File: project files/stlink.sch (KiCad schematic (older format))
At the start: 62 parts, among them J1 USB_C_Receptacle_USB2.0, J2 SWD, J3 SELF, J4 TARGET, Q1 MMBT9013, U1 STM32F103CBTx, U2 AMS1117-3.3, Y1 8MHz

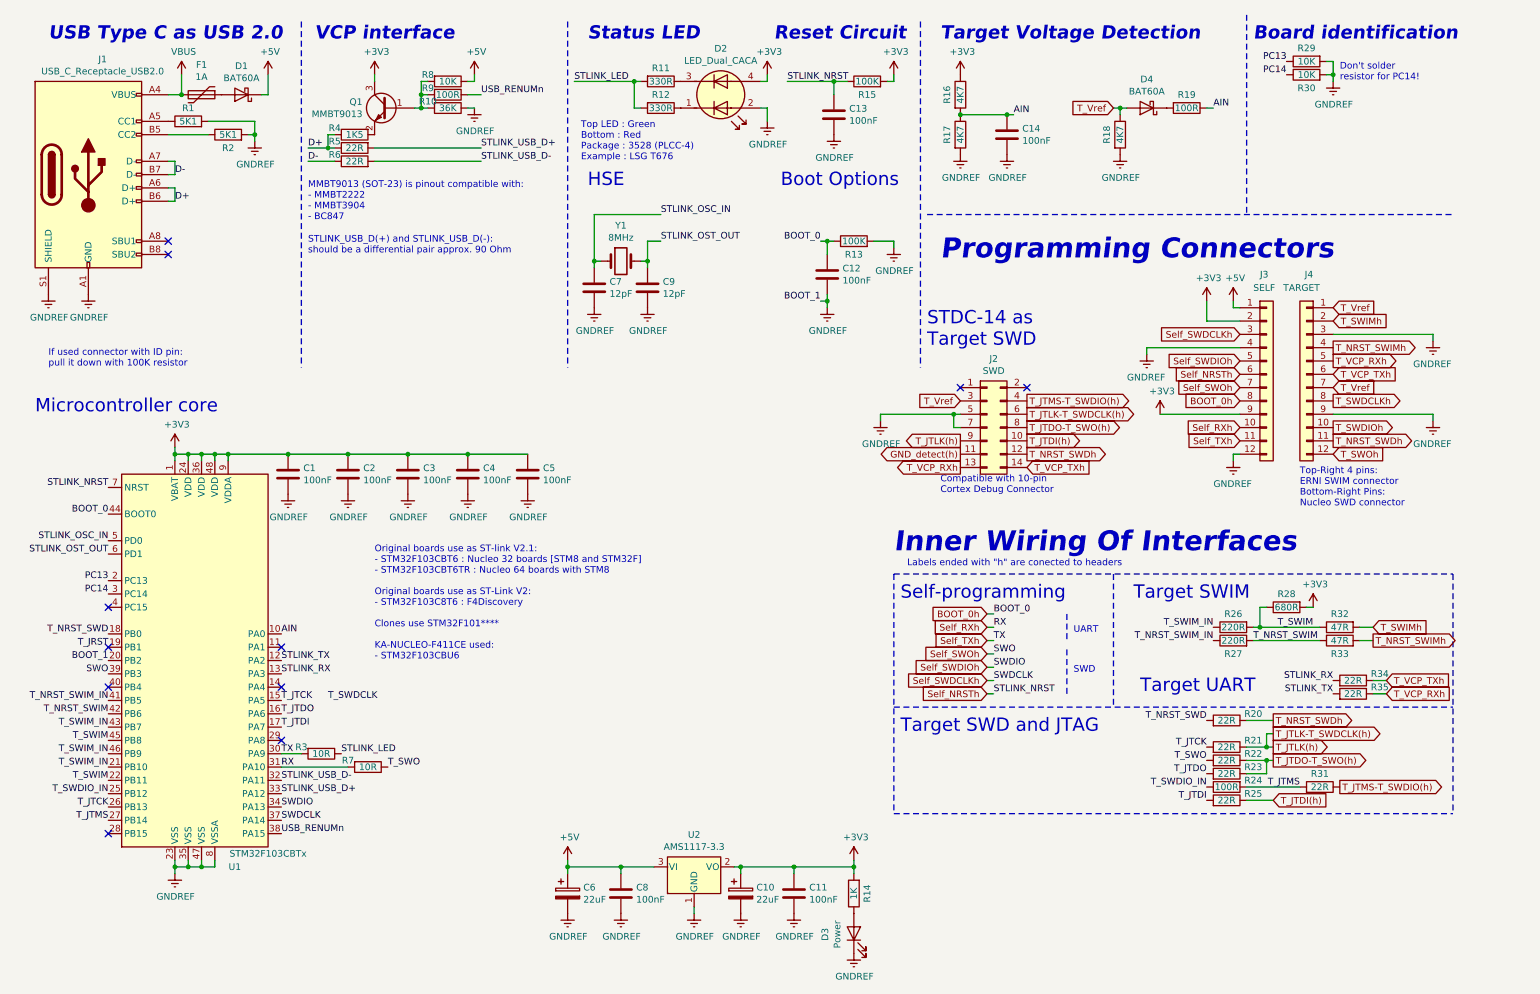
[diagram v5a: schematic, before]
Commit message: USB Type C shield fix
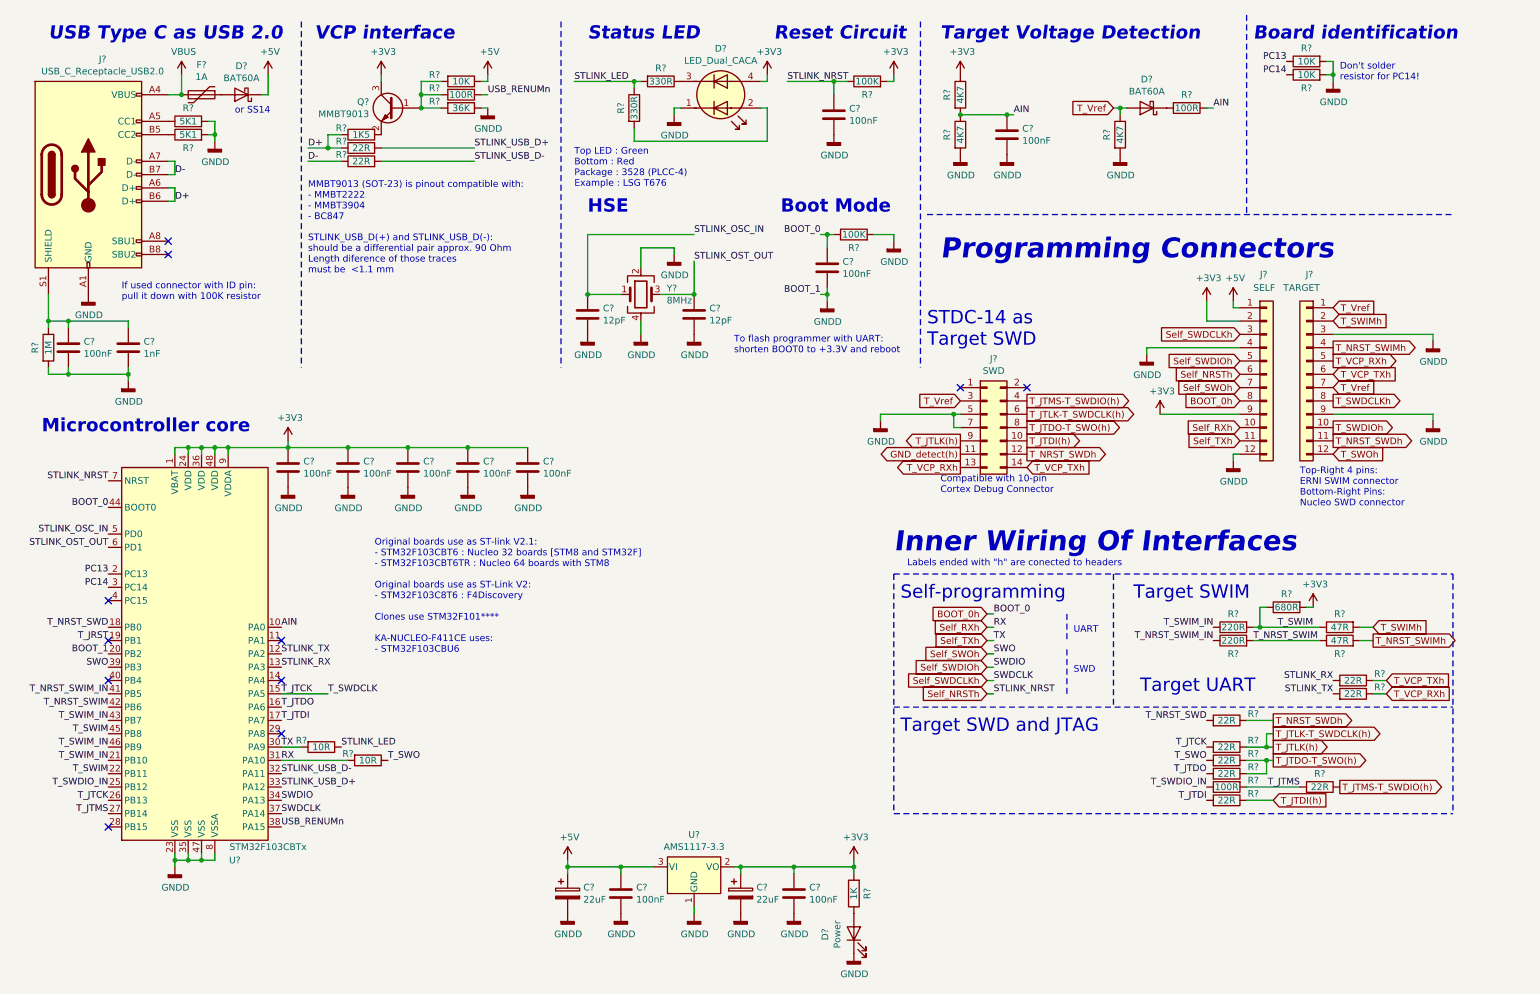
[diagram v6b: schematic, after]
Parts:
- removed Y1: 8MHz, Crystal:Crystal_HC49-4H_Vertical, symbol Device:Crystal
- added C?: 1nF, Capacitor_SMD:C_0603_1608Metric, symbol Device:C
- added C?: 100nF, Capacitor_SMD:C_0603_1608Metric, symbol Device:C
- added R?: 1M, Resistor_SMD:R_0603_1608Metric_Pad1.05x0.95mm_HandSolder, symbol Device:R
- added Y?: 8MHz, Crystal:Crystal_SMD_Abracon_ABM8G-4Pin_3.2x2.5mm, symbol Device:Crystal_GND24
- renumbered C9 to C?, C7 to C?, C13 to C?, C12 to C?, C14 to C?, C1 to C?, C2 to C?, C3 to C?, C4 to C?, C5 to C?, C10 to C?, C6 to C?, C11 to C?, C8 to C?, D3 to D?, D2 to D?, D4 to D?, D1 to D?, F1 to F?, J1 to J?, J2 to J?, J3 to J?, J4 to J?, Q1 to Q?, R2 to R?, R1 to R?, R6 to R?, R5 to R?, R4 to R?, R9 to R?, R8 to R?, R10 to R?, R11 to R?, R12 to R?, R27 to R?, R26 to R?, R33 to R?, R32 to R?, R29 to R?, R15 to R?, R13 to R?, R16 to R?, R17 to R?, R28 to R?, R30 to R?, R18 to R?, R19 to R?, R22 to R?, R31 to R?, R21 to R?, R20 to R?, R24 to R?, R14 to R?, R7 to R?, R3 to R?, R35 to R?, R34 to R?, R23 to R?, R25 to R?, U1 to U?, U2 to U?
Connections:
- net STLINK_LED: now also R?.1; no longer R?.2
- net STLINK_OSC_IN: now also Y?.1
- net STLINK_OST_OUT: now also Y?.3
- net GNDD: now reaches D?.1 (A1)
- net GNDD: now also C?.2, C?.2, C?.2, C?.2, C?.2, C?.2, C?.2, C?.2, C?.2, C?.2, C?.2, C?.2, C?.2, C?.2, D?.1 (K), J?.12 (Pin_12), J?.3 (Pin_3), J?.4 (Pin_4), J?.5 (Pin_5), J?.7 (Pin_7), J?.9 (Pin_9), J?.A1 (GND), J?.A12 (GND), J?.B1 (GND), J?.B12 (GND), R?.1, R?.2, R?.2, R?.2, R?.2, R?.2, R?.2, R?.2, U?.1 (GND), U?.20 (PB2), U?.23 (VSS), U?.35 (VSS), U?.47 (VSS), U?.8 (VSSA), C?.2, C?.2, R?.2, Y?.2, Y?.4; no longer R?.1
- removed net GNDREF: C?.2, C?.2, C?.2, C?.2, C?.2, C?.2, C?.2, C?.2, C?.2, C?.2, C?.2, C?.2, C?.2, C?.2, D?.1 (K), D?.2 (K1), J?.12 (Pin_12), J?.3 (Pin_3), J?.4 (Pin_4), J?.5 (Pin_5), J?.7 (Pin_7), J?.9 (Pin_9), J?.A1 (GND), J?.A12 (GND), J?.B1 (GND), J?.B12 (GND), J?.S1 (SHIELD), R?.1, R?.2, R?.2, R?.2, R?.2, R?.2, R?.2, R?.2, U?.1 (GND), U?.20 (PB2), U?.23 (VSS), U?.35 (VSS), U?.47 (VSS), U?.8 (VSSA)
- new net: C?.1, C?.1, J?.S1 (SHIELD), R?.1
- new net: D?.2 (K1), R?.2
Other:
- note added: "Boot Mode"
- note added: "Original boards use as ST-link V2.1:\n- STM32F103CBT6 : Nucleo 32 boards [STM8 and STM32F]\n- STM32F103CBT6TR : Nucleo 64 boards with STM8\n\nOriginal boards use as ST-Link V2:\n- STM32F103C8T6 : F4Discovery\n\nClones use STM32F101****\n\nKA-NUCLEO-F411CE uses:\n- STM32F103CBU6"
- note added: "STLINK_USB_D(+) and STLINK_USB_D(-):\nshould be a differential pair approx. 90 Ohm\nLength diference of those traces \nmust be <1.1 mm"
- note added: "To flash programmer with UART:\nshorten BOOT0 to +3.3V and reboot"
- note added: "or SS14"
- note removed: "Boot Options"
- note removed: "Original boards use as ST-link V2.1:\n- STM32F103CBT6 : Nucleo 32 boards [STM8 and STM32F]\n- STM32F103CBT6TR : Nucleo 64 boards with STM8\n\nOriginal boards use as ST-Link V2:\n- STM32F103C8T6 : F4Discovery\n\nClones use STM32F101****\n\nKA-NUCLEO-F411CE used:\n- STM32F103CBU6"
- note removed: "STLINK_USB_D(+) and STLINK_USB_D(-):\nshould be a differential pair approx. 90 Ohm"
- moved on the sheet: C?, Q?, R?, U?

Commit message: Update stlink.sch
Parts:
- removed R?: 10K, Resistor_SMD:R_0603_1608Metric_Pad1.05x0.95mm_HandSolder, symbol Device:R
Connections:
- net AIN: now also C?.2; no longer C?.1
- net GNDD: now also C?.1, R?.1; no longer C?.2, R?.2, R?.2
- net PC13: no longer names the net of U?.2 (PC13)
- net PC13: now also R?.2; no longer R?.1
- net PC14: no longer names the net of U?.3 (PC14)
- no-connect marks 11 -> 12
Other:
- note added: "STDC-14 as\nTarget SWD + VCP"
- note added: "Target Voltage\nDetection"
- note removed: "Board identification"
- note removed: "Don't solder\nresistor for PC14!"
- note removed: "STDC-14 as\nTarget SWD"
- note removed: "Target Voltage Detection"
- moved on the sheet: C?, D?, J?, R?, Y?

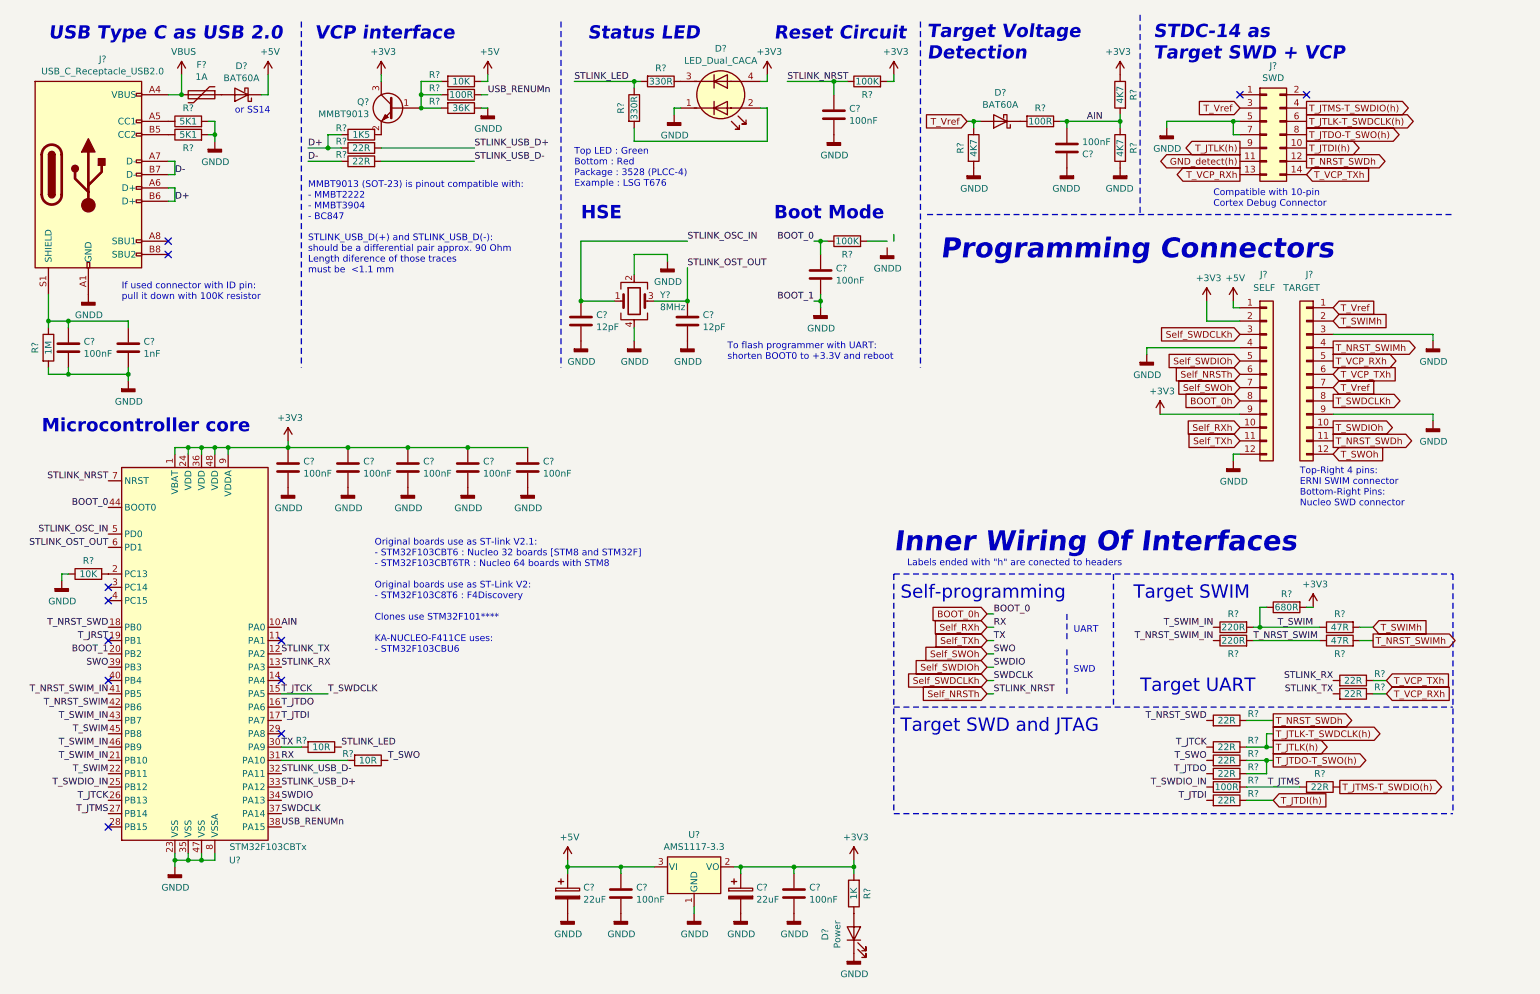
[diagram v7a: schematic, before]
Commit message: Added possibility to power target from programmer
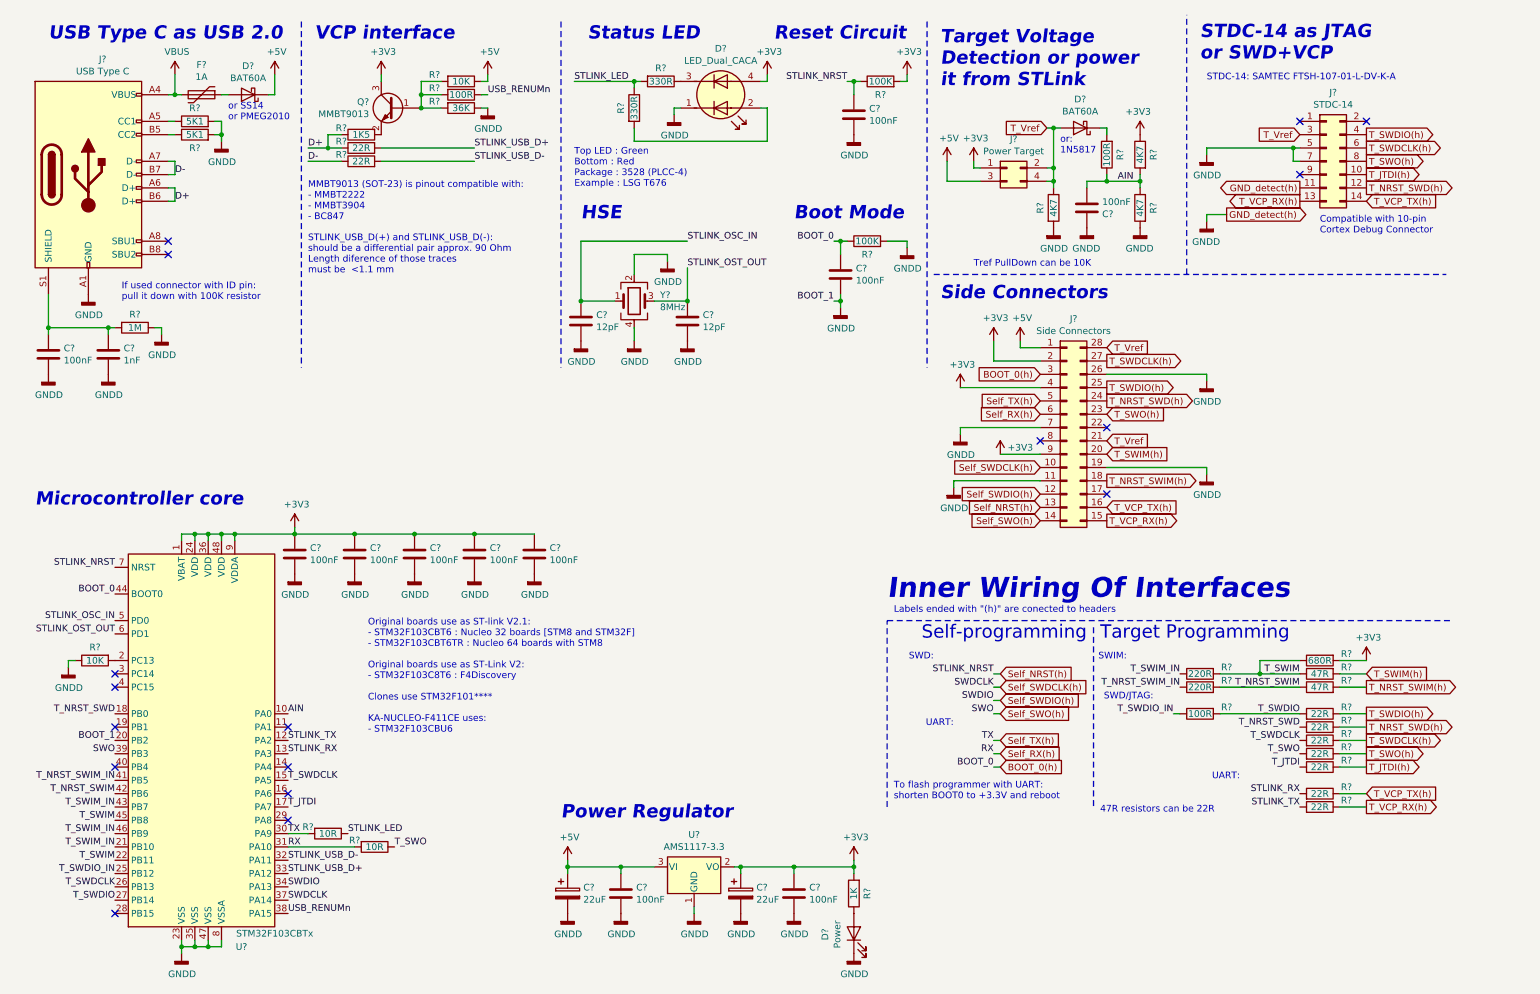
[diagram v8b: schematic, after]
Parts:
- removed J?: SELF, Connector_PinHeader_2.54mm:PinHeader_1x12_P2.54mm_Vertical, symbol Connector_Generic:Conn_01x12
- removed J?: TARGET, Connector_PinHeader_2.54mm:PinHeader_1x12_P2.54mm_Vertical, symbol Connector_Generic:Conn_01x12
- removed R? (x2): 22R, Resistor_SMD:R_0603_1608Metric_Pad1.05x0.95mm_HandSolder, symbol Device:R
- added J?: Power Target, Connector_PinHeader_2.54mm:PinHeader_2x02_P2.54mm_Vertical, symbol Connector_Generic:Conn_02x02_Odd_Even
- added J?: Side Connectors, Package_DIP:DIP-28_W15.24mm_Socket, symbol Connector_Generic:Conn_02x14_Counter_Clockwise
- added R?: 22R, Resistor_SMD:R_0805_2012Metric, symbol Device:R
- C? (x7): footprint Capacitor_SMD:C_0603_1608Metric_Pad1.05x0.95mm_HandSolder -> Capacitor_SMD:C_0805_2012Metric
- C? (x7): footprint Capacitor_SMD:C_0603_1608Metric -> Capacitor_SMD:C_0805_2012Metric
- F?: footprint Fuse:Fuse_1812_4532Metric -> Resistor_SMD:R_1206_3216Metric
- J?: value USB_C_Receptacle_USB2.0 -> USB Type C
- J?: value SWD -> STDC-14
- R? (x33): footprint Resistor_SMD:R_0603_1608Metric_Pad1.05x0.95mm_HandSolder -> Resistor_SMD:R_0805_2012Metric
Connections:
- net GND_detect(h) is gone; now on net GNDD: J?.11 (Pin_11)
- net +3V3: now also J?.1 (Pin_1), J?.2 (Pin_2), J?.4 (Pin_4), J?.9 (Pin_9)
- net +5V: now also J?.1 (Pin_1), J?.3 (Pin_3)
- net GNDD: now also R?.1, R?.2, J?.11 (Pin_11), J?.19 (Pin_19), J?.26 (Pin_26), J?.7 (Pin_7); no longer R?.2
- net T_JTDI: now also R?.2
- net T_JTDI(h): now also R?.1
- net T_Vref: now also J?.2 (Pin_2), J?.21 (Pin_21), J?.28 (Pin_28), J?.4 (Pin_4)
- net at C?.1, C?.1, J?.S1 (SHIELD): now also R?.2; no longer R?.1
- net BOOT_0h renamed BOOT_0(h)
- net BOOT_0(h): now also J?.3 (Pin_3)
- net Self_NRSTh renamed Self_NRST(h)
- net Self_NRST(h): now also J?.13 (Pin_13)
- net Self_RXh renamed Self_RX(h)
- net Self_RX(h): now also J?.6 (Pin_6)
- net Self_SWDCLKh renamed Self_SWDCLK(h)
- net Self_SWDCLK(h): now also J?.10 (Pin_10)
- net Self_SWDIOh renamed Self_SWDIO(h)
- net Self_SWDIO(h): now also J?.12 (Pin_12)
- net Self_SWOh renamed Self_SWO(h)
- net Self_SWO(h): now also J?.14 (Pin_14)
- net Self_TXh renamed Self_TX(h)
- net Self_TX(h): now also J?.5 (Pin_5)
- net T_JRST: no longer names the net of U?.19 (PB1)
- net T_JTCK renamed T_SWDCLK
- net T_JTDO: no longer names the net of U?.16 (PA6)
- net T_JTDO-T_SWO(h) renamed T_SWO(h)
- net T_SWO(h): now also J?.23 (Pin_23)
- net T_JTLK(h) renamed T_SWDCLK(h)
- net T_SWDCLK(h): now also J?.27 (Pin_27); no longer J?.9 (Pin_9)
- net T_JTMS renamed T_SWDIO
- net T_JTMS-T_SWDIO(h) renamed T_SWDIO(h)
- net T_SWDIO(h): now also J?.25 (Pin_25)
- net T_NRST_SWDh renamed T_NRST_SWD(h)
- net T_NRST_SWD(h): now also J?.24 (Pin_24)
- net T_NRST_SWIMh renamed T_NRST_SWIM(h)
- net T_NRST_SWIM(h): now also J?.18 (Pin_18)
- net T_SWIMh renamed T_SWIM(h)
- net T_SWIM(h): now also J?.20 (Pin_20)
- net T_VCP_RXh renamed T_VCP_RX(h)
- net T_VCP_RX(h): now also J?.15 (Pin_15)
- net T_VCP_TXh renamed T_VCP_TX(h)
- net T_VCP_TX(h): now also J?.16 (Pin_16)
- no-connect marks 12 -> 17
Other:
- note added: "47R resistors can be 22R"
- note added: "Labels ended with "(h)" are conected to headers"
- note added: "Power Regulator"
- note added: "STDC-14 as JTAG \nor SWD+VCP"
- note added: "STDC-14: SAMTEC FTSH-107-01-L-DV-K-A"
- note added: "SWD/JTAG:"
- note added: "SWD:"
- note added: "SWIM:"
- note added: "Side Connectors"
- note added: "Target Programming"
- note added: "Target Voltage\nDetection or power\nit from STLink"
- note added: "Tref PullDown can be 10K"
- note added: "UART:"
- note added: "or SS14\nor PMEG2010"
- note added: "or:\n1N5817"
- note removed: "Labels ended with "h" are conected to headers"
- note removed: "Programming Connectors"
- note removed: "STDC-14 as\nTarget SWD + VCP"
- note removed: "SWD"
- note removed: "Target SWD and JTAG"
- note removed: "Target SWIM"
- note removed: "Target UART"
- note removed: "Target Voltage\nDetection"
- note removed: "Top-Right 4 pins:\nERNI SWIM connector\nBottom-Right Pins: \nNucleo SWD connector"
- note removed: "UART"
- note removed: "or SS14"
- moved on the sheet: C?, D?, J?, R?, U?
